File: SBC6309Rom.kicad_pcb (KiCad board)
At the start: 2 copper layers, 49.4 x 40.8 mm, 10 parts, among them J1 Address, J2 Device, J3 Clock, J4 Power, J5 Data, J6 Address select, U1 28C256, U6 GAL16V8

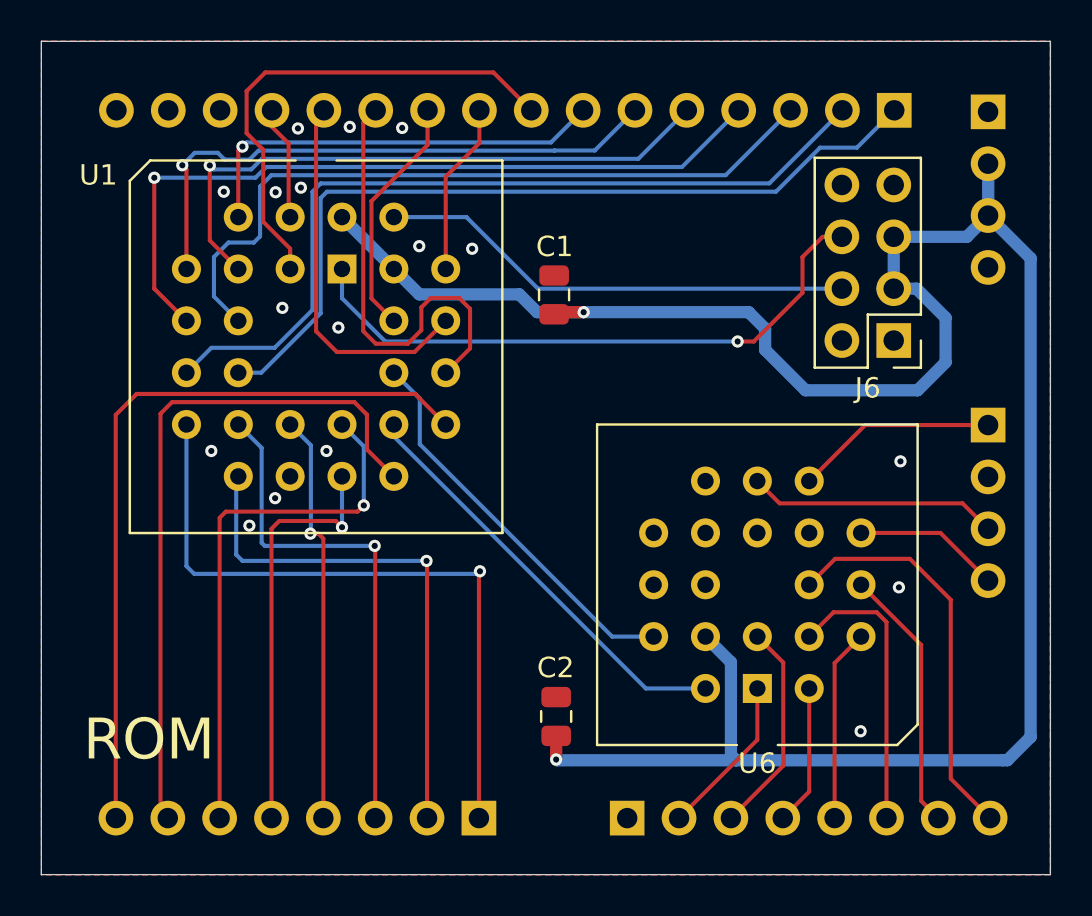
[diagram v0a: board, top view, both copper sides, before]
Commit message: fix rom footprint
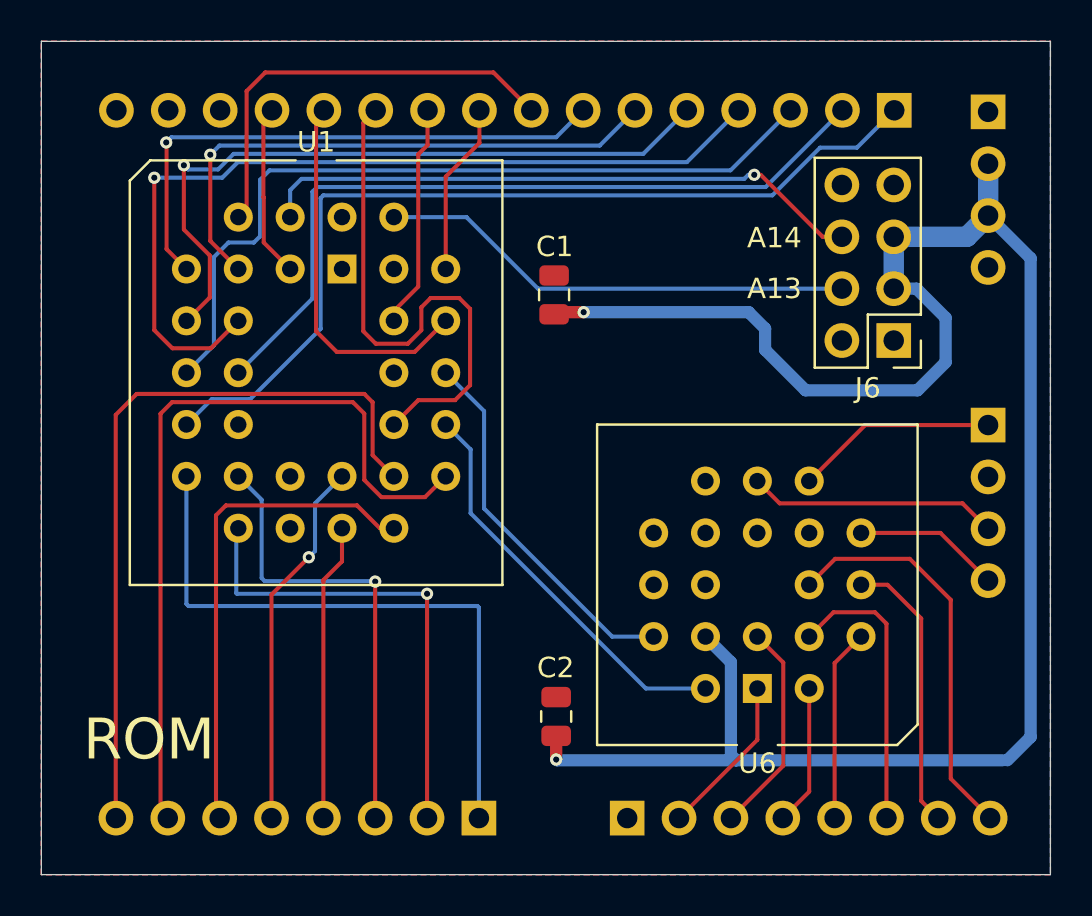
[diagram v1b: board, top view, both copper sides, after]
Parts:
- U1: footprint Package_LCC:PLCC-28_THT-Socket -> Package_LCC:PLCC-32_THT-Socket
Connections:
- J6 pad 4: Net-(J6-Pin_4) -> /A13page
- J6 pad 6: Net-(J6-Pin_6) -> /A14page
- U1 pad 1: Net-(J6-Pin_6) -> unconnected-(U1-DC-Pad1)
- U1 pad 10: /A0 -> /A1
- U1 pad 11: /D0 -> /A0
- U1 pad 12: /D1 -> unconnected-(U1-NC-Pad12)
- U1 pad 13: /D2 -> /D0
- U1 pad 14: GND -> /D1
- U1 pad 15: /D3 -> /D2
- U1 pad 16: /D4 -> GND
- U1 pad 17: /D5 -> unconnected-(U1-DC-Pad17)
- U1 pad 18: /D6 -> /D3
- U1 pad 19: /D7 -> /D4
- U1 pad 2: /A12 -> /A14page
- U1 pad 20: /~{CS} -> /D5
- U1 pad 21: /A10 -> /D6
- U1 pad 22: /~{OE} -> /D7
- U1 pad 23: /A11 -> /~{CS}
- U1 pad 24: /A9 -> /A10
- U1 pad 25: /A8 -> /~{OE}
- U1 pad 26: Net-(J6-Pin_4) -> unconnected-(U1-NC-Pad26)
- U1 pad 27: +5V -> /A11
- U1 pad 28: +5V -> /A9
- U1 pad 3: /A7 -> /A12
- U1 pad 4: /A6 -> /A7
- U1 pad 5: /A5 -> /A6
- U1 pad 6: /A4 -> /A5
- U1 pad 7: /A3 -> /A4
- U1 pad 8: /A2 -> /A3
- U1 pad 9: /A1 -> /A2
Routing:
- net /A14page: track 0.00 -> 30.0 mm, vias 0 -> 1
- net Net-(J6-Pin_6): track 29.9 -> 0.00 mm, vias 1 -> 0
- net Net-(J6-Pin_4): track 23.4 -> 0.00 mm
- net /A13page: track 0.00 -> 23.4 mm
- net /A6: track 21.0 -> 27.7 mm
- net /D3: track 20.2 -> 14.6 mm, vias 1 -> 0
- net /A3: track 37.7 -> 42.5 mm
- net /A10: track 22.0 -> 26.6 mm
- net /D6: track 34.1 -> 38.4 mm
- net /A4: track 30.3 -> 34.5 mm
- net /A0: track 40.8 -> 44.8 mm
- net /A7: track 24.7 -> 21.4 mm
- net /A12: track 5.60 -> 8.49 mm
- net /A1: track 40.8 -> 38.0 mm
- net /A2: track 36.3 -> 39.1 mm
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- added copper zone on In1.Cu, net GND
- added copper zone on In2.Cu, net GND
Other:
- copper layers 2 -> 4
- board text added: "A13"
- board text added: "A14"
